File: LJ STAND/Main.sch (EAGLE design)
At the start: 211 parts, among them Q1 200mA/50V

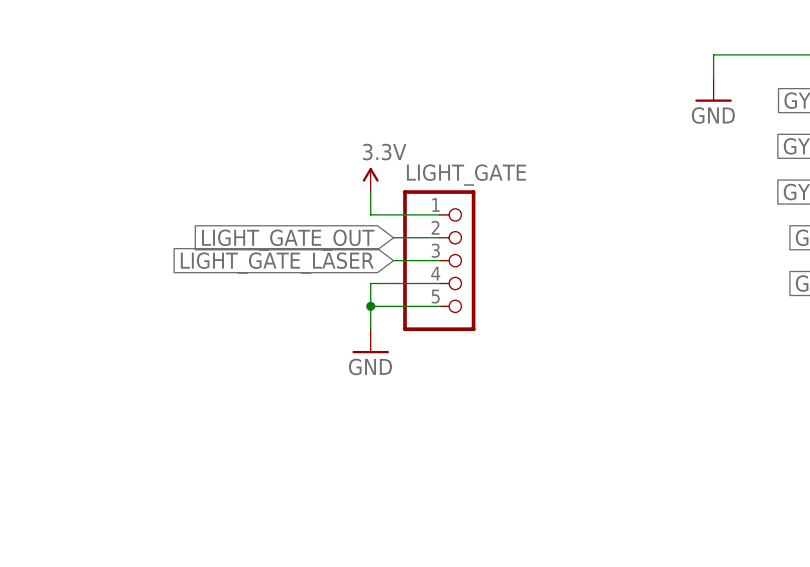
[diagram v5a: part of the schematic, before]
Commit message: Light gate plug labels
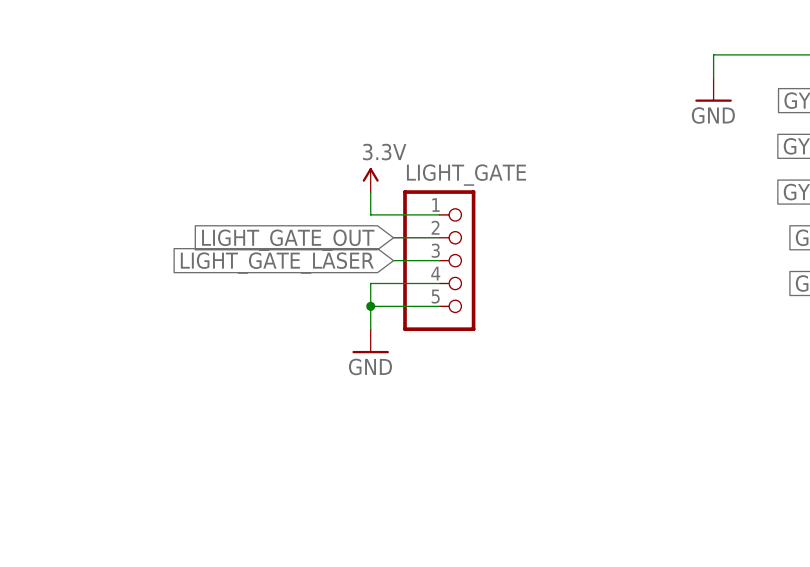
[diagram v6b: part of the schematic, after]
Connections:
- removed net N$61: LIGHT_GATE.4
- net GND: now also LIGHT_GATE.4
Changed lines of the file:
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@@
 <pinref part="GND99" gate="1" pin="GND"/>
 <wire x1="-68.58" y1="-10.16" x2="-68.58" y2="-7.62" width="0.1524" layer="91"/>
-<wire x1="-68.58" y1="-7.62" x2="-66.04" y2="-7.62" width="0.1524" layer="91"/>
 <junction x="-68.58" y="-10.16"/>
+<pinref part="LIGHT_GATE" gate="G$1" pin="4"/>
+<wire x1="-60.96" y1="-7.62" x2="-68.58" y2="-7.62" width="0.1524" layer="91"/>
 </segment>
 </net>
@@
 </segment>
 </net>
-<net name="N$61" class="0">
-<segment>
-<pinref part="LIGHT_GATE" gate="G$1" pin="4"/>
-<wire x1="-60.96" y1="-7.62" x2="-66.04" y2="-7.62" width="0.1524" layer="91"/>
-</segment>
-</net>

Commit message: Main edits, light gate pcbs
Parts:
- added C18, C19: 0.1uF, SparkFun-Capacitors:CAP0805
- BT_DEBUG_LED, BT_IRC_LED: value (none) -> BLUE
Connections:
- net 3.3V: now also C18.1, C19.1
- net GND: now also C18.2, C19.2
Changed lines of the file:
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@@
 <?xml version="1.0" encoding="utf-8"?>
 <!DOCTYPE eagle SYSTEM "eagle.dtd">
-<eagle version="8.6.3">
+<eagle version="8.7.0">
 <drawing>
 <settings>
@@
 <part name="SUPPLY7" library="SparkFun-Aesthetics" deviceset="3.3V" device=""/>
 <part name="R5" library="SparkFun-Resistors" deviceset="RESISTOR" device="0603-RES" value="330"/>
-<part name="BT_IRC_LED" library="SparkFun-LED" library_urn="urn:adsk.eagle:library:1981965" deviceset="LED" device="0603" package3d_urn="urn:adsk.eagle:package:1982017/2"/>
+<part name="BT_IRC_LED" library="SparkFun-LED" library_urn="urn:adsk.eagle:library:1981965" deviceset="LED" device="0603" package3d_urn="urn:adsk.eagle:package:1982017/2" value="BLUE"/>
 <part name="R6" library="SparkFun-Resistors" deviceset="RESISTOR" device="0603-RES" value="330"/>
-<part name="BT_DEBUG_LED" library="SparkFun-LED" library_urn="urn:adsk.eagle:library:1981965" deviceset="LED" device="0603" package3d_urn="urn:adsk.eagle:package:1982017/2"/>
+<part name="BT_DEBUG_LED" library="SparkFun-LED" library_urn="urn:adsk.eagle:library:1981965" deviceset="LED" device="0603" package3d_urn="urn:adsk.eagle:package:1982017/2" value="BLUE"/>
 <part name="P1" library="VNH5050ATR-E" deviceset="SOP50P1030X247-36N" device=""/>
 <part name="GND10" library="SparkFun-Aesthetics" deviceset="GND" device=""/>
@@
 <part name="R61" library="SparkFun-Resistors" deviceset="RESISTOR" device="0603-RES" value="1K"/>
 <part name="R62" library="SparkFun-Resistors" deviceset="RESISTOR" device="0603-RES" value="1K"/>
+<part name="C18" library="SparkFun-Capacitors" deviceset="CAP" device="0805" value="0.1uF"/>
+<part name="C19" library="SparkFun-Capacitors" deviceset="CAP" device="0805" value="0.1uF"/>
+<part name="GND100" library="SparkFun-Aesthetics" deviceset="GND" device=""/>
+<part name="GND101" library="SparkFun-Aesthetics" deviceset="GND" device=""/>
 </parts>
 <sheets>
@@
 <instance part="R61" gate="G$1" x="421.64" y="101.6"/>
 <instance part="R62" gate="G$1" x="452.12" y="101.6"/>
+<instance part="C18" gate="G$1" x="-132.08" y="-25.4"/>
+<instance part="C19" gate="G$1" x="-132.08" y="-91.44"/>
+<instance part="GND100" gate="1" x="-132.08" y="-33.02"/>
+<instance part="GND101" gate="1" x="-132.08" y="-99.06"/>
 </instances>
 <busses>
@@
 <wire x1="-60.96" y1="-7.62" x2="-68.58" y2="-7.62" width="0.1524" layer="91"/>
 </segment>
+<segment>
+<pinref part="C19" gate="G$1" pin="2"/>
+<pinref part="GND101" gate="1" pin="GND"/>
+<wire x1="-132.08" y1="-93.98" x2="-132.08" y2="-96.52" width="0.1524" layer="91"/>
+</segment>
+<segment>
+<pinref part="C18" gate="G$1" pin="2"/>
+<pinref part="GND100" gate="1" pin="GND"/>
+<wire x1="-132.08" y1="-27.94" x2="-132.08" y2="-30.48" width="0.1524" layer="91"/>
+</segment>
 </net>
 <net name="N$12" class="0">
@@
 </segment>
 <segment>
-<wire x1="-147.32" y1="-17.78" x2="-127" y2="-17.78" width="0.1524" layer="91"/>
+<wire x1="-147.32" y1="-17.78" x2="-132.08" y2="-17.78" width="0.1524" layer="91"/>
+<wire x1="-132.08" y1="-17.78" x2="-127" y2="-17.78" width="0.1524" layer="91"/>
 <wire x1="-127" y1="-17.78" x2="-127" y2="-15.24" width="0.1524" layer="91"/>
 <pinref part="SUPPLY6" gate="G$1" pin="3.3V"/>
 <pinref part="BT_IRC" gate="G$1" pin="VCC"/>
-</segment>
-<segment>
-<wire x1="-147.32" y1="-83.82" x2="-127" y2="-83.82" width="0.1524" layer="91"/>
+<pinref part="C18" gate="G$1" pin="1"/>
+<wire x1="-132.08" y1="-20.32" x2="-132.08" y2="-17.78" width="0.1524" layer="91"/>
+<junction x="-132.08" y="-17.78"/>
+</segment>
+<segment>
+<wire x1="-147.32" y1="-83.82" x2="-132.08" y2="-83.82" width="0.1524" layer="91"/>
+<wire x1="-132.08" y1="-83.82" x2="-127" y2="-83.82" width="0.1524" layer="91"/>
 <wire x1="-127" y1="-83.82" x2="-127" y2="-81.28" width="0.1524" layer="91"/>
 <pinref part="SUPPLY7" gate="G$1" pin="3.3V"/>
 <pinref part="BT_DEBUG" gate="G$1" pin="VCC"/>
-</segment>
-<segment>
+<pinref part="C19" gate="G$1" pin="1"/>
+<wire x1="-132.08" y1="-86.36" x2="-132.08" y2="-83.82" width="0.1524" layer="91"/>
+<junction x="-132.08" y="-83.82"/>
+</segment>
+<segment>

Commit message: Finalisation of gyro, encoder and light boards + gerbers, silkscreen fixes
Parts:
- C11, C12, C13, C14, C15, C16, C17, C18, C19, C2, C3, C38, C39, C4, C40, C41, C42, C43, C44, C45, C46, C47, C48, C49, C5, C50, C51, C52, C53, C54, C55, C56, C57, C58, C59, C6, C60, C61, C62, C63, C64, C65, C66, C67, C68, C69, C70, C71, C72, C73: device SparkFun-Capacitors:CAP0805 -> SparkFun-Capacitors:CAP0603-CAP
